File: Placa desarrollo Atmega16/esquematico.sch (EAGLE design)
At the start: 34 parts, among them IC1 MEGA16-P, IC2 7805DT, IC3 7805DT, Q1 16MHz

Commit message: PCB sin rutear
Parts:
- removed C13: 100nF, rcl:C-EUC1206
- removed C14: 10uF, rcl:CPOL-EUE2,5-6E
- removed Q1: 16MHz, crystal:CRYSTALHC33U-V
- added JP2: (no value), jumper:JP1E
- added Q2: 16MHz, crystal:CRYSTALHC49S
- added X1: PN61729-S, con-berg:PN61729-S
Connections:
- removed net N$4: R5.2
- removed net N$7: C13.1, C14.+, IC2.VI
- new net PA6: IC1.(ADC6)PA6, SV2.14
- net AREF: now also SV2.12
- net GND: now also SV2.11, X1.4, X1.S1, X1.S2; no longer C13.2, C14.-
- net N$5: now also IC2.VI, JP2.2; no longer C10.+, C9.1
- net PA0: now also SV2.20
- net PA1: now also SV2.19
- net PA2: now also SV2.18
- net PA3: now also SV2.17
- net PA4: now also SV2.16
- net PA5: now also SV2.15
- net PA7: now also SV2.13; no longer IC1.(ADC6)PA6
- net PC0: now also SV2.2
- net PC1: now also SV2.3
- net PC2: now also SV2.4
- net PC3: now also SV2.5
- net PC4: now also SV2.6
- net PC5: now also SV2.7
- net PC6: now also SV2.8
- net PC7: now also SV2.9
- net PD7: now also SV2.1
- net VCC_5V: now also C10.+, C9.1, R5.2, SV2.10, X1.1
- net VIN: now also JP2.1
- net XTAL1: now also Q2.1; no longer Q1.2
- net XTAL2: now also Q2.2; no longer Q1.1
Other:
- moved on the sheet: R5

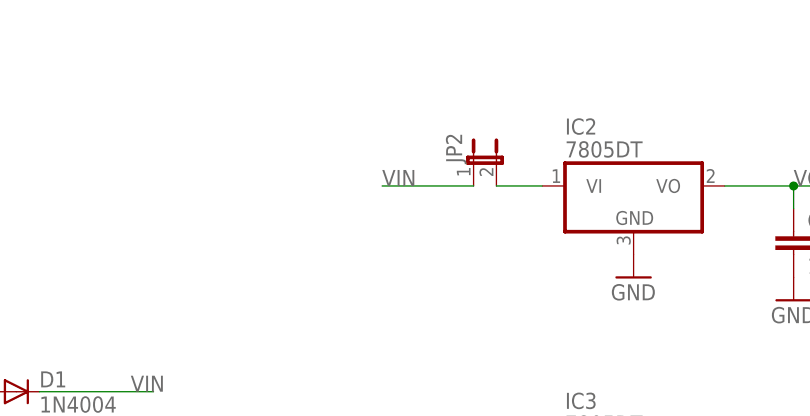
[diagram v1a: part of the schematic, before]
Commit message: Modifique el jumper del lm7833
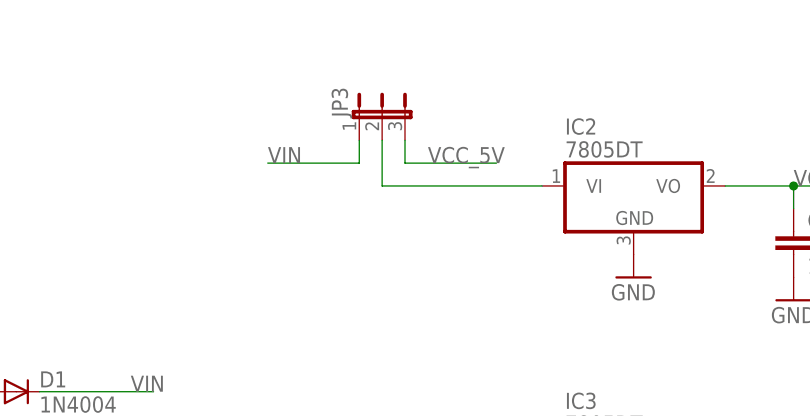
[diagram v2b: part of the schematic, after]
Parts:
- removed JP2: (no value), jumper:JP1E
- added JP3: (no value), jumper:JP2E
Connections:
- net N$5: now also JP3.2; no longer JP2.2
- net VCC_5V: now also JP3.3
- net VIN: now also JP3.1; no longer JP2.1
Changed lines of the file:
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@@
 <part name="GND22" library="supply1" deviceset="GND" device=""/>
 <part name="Q2" library="crystal" deviceset="CRYSTAL" device="HC49S" value="16MHz"/>
-<part name="JP2" library="jumper" deviceset="JP1E" device=""/>
+<part name="JP3" library="jumper" deviceset="JP2E" device=""/>
 </parts>
 <sheets>
@@
 <instance part="GND22" gate="1" x="-48.26" y="149.86"/>
 <instance part="Q2" gate="G$1" x="-38.1" y="58.42"/>
-<instance part="JP2" gate="A" x="15.24" y="147.32"/>
+<instance part="JP3" gate="1" x="5.08" y="152.4"/>
 </instances>
 <busses>
@@
 <label x="-25.4" y="27.94" size="1.778" layer="95"/>
 </segment>
+<segment>
+<pinref part="JP3" gate="1" pin="3"/>
+<wire x1="7.62" y1="149.86" x2="7.62" y2="147.32" width="0.1524" layer="91"/>
+<wire x1="7.62" y1="147.32" x2="17.78" y2="147.32" width="0.1524" layer="91"/>
+<label x="10.16" y="147.32" size="1.778" layer="95"/>
+</segment>
 </net>
 <net name="MOSI" class="0">
@@
 </segment>
 <segment>
-<pinref part="JP2" gate="A" pin="1"/>
-<wire x1="15.24" y1="144.78" x2="5.08" y2="144.78" width="0.1524" layer="91"/>
-<label x="5.08" y="144.78" size="1.778" layer="95"/>
+<wire x1="2.54" y1="147.32" x2="-7.62" y2="147.32" width="0.1524" layer="91"/>
+<label x="-7.62" y="147.32" size="1.778" layer="95"/>
+<pinref part="JP3" gate="1" pin="1"/>
+<wire x1="2.54" y1="149.86" x2="2.54" y2="147.32" width="0.1524" layer="91"/>
 </segment>
 </net>
@@
 <net name="N$5" class="0">
 <segment>
-<pinref part="JP2" gate="A" pin="2"/>
 <pinref part="IC2" gate="A1" pin="VI"/>
-<wire x1="17.78" y1="144.78" x2="22.86" y2="144.78" width="0.1524" layer="91"/>
-</segment>
-</net>
+<pinref part="JP3" gate="1" pin="2"/>
+<wire x1="5.08" y1="149.86" x2="5.08" y2="144.78" width="0.1524" layer="91"/>
+<wire x1="5.08" y1="144.78" x2="22.86" y2="144.78" width="0.1524" layer="91"/>
+</segment>
+</net>

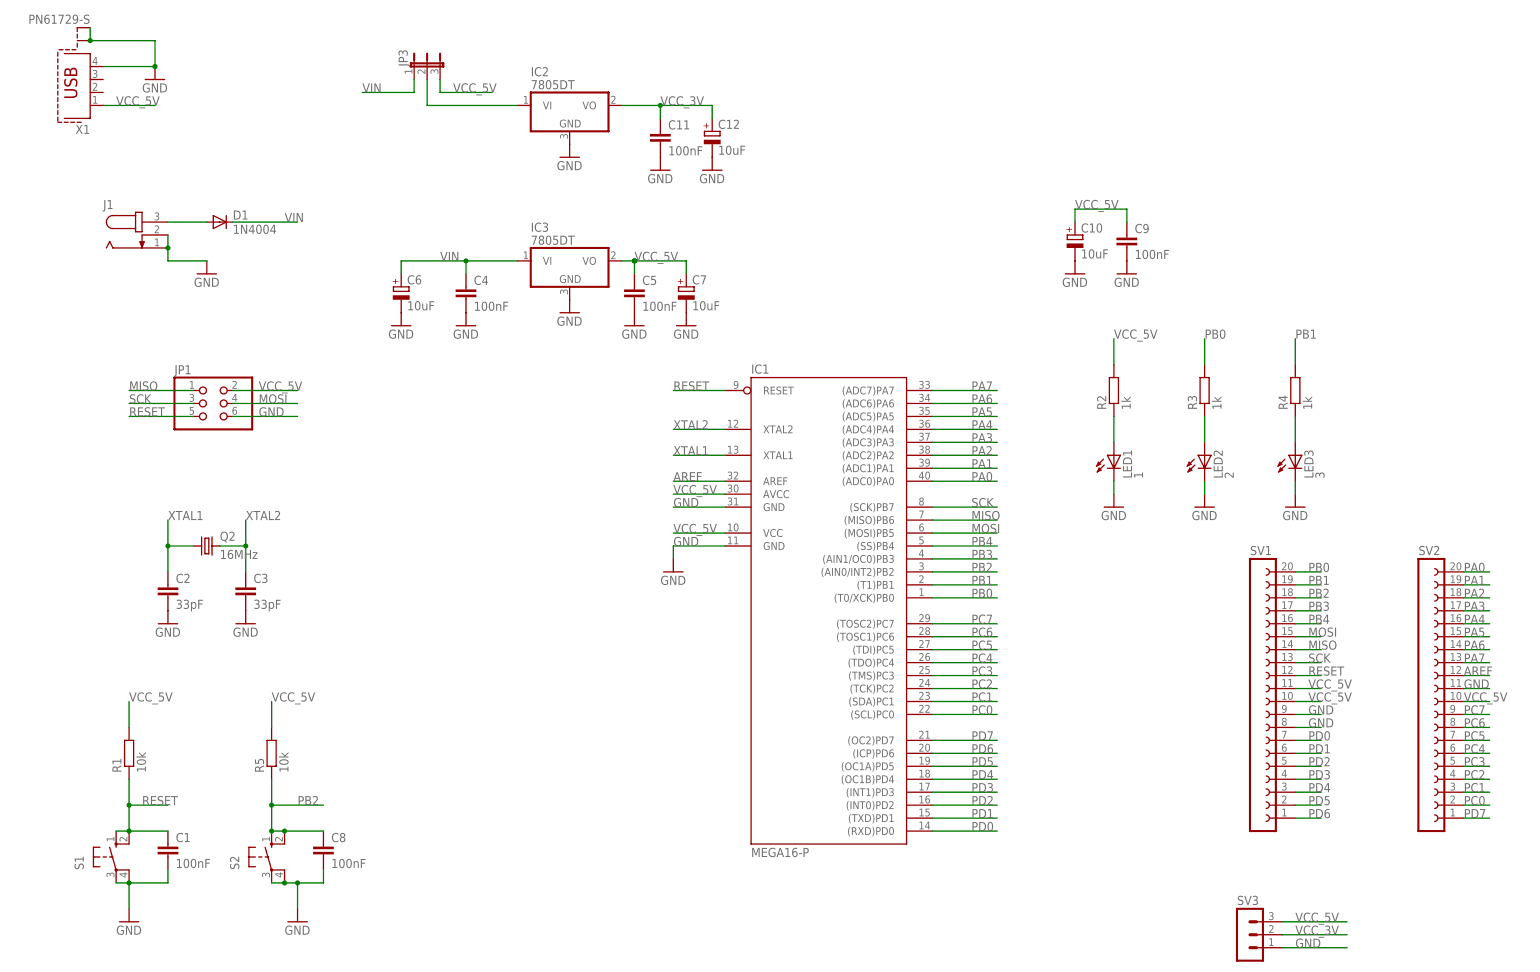
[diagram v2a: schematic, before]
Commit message: Modifique el ancho de las pistas. Hay algunos problemas con la interconexion de masas
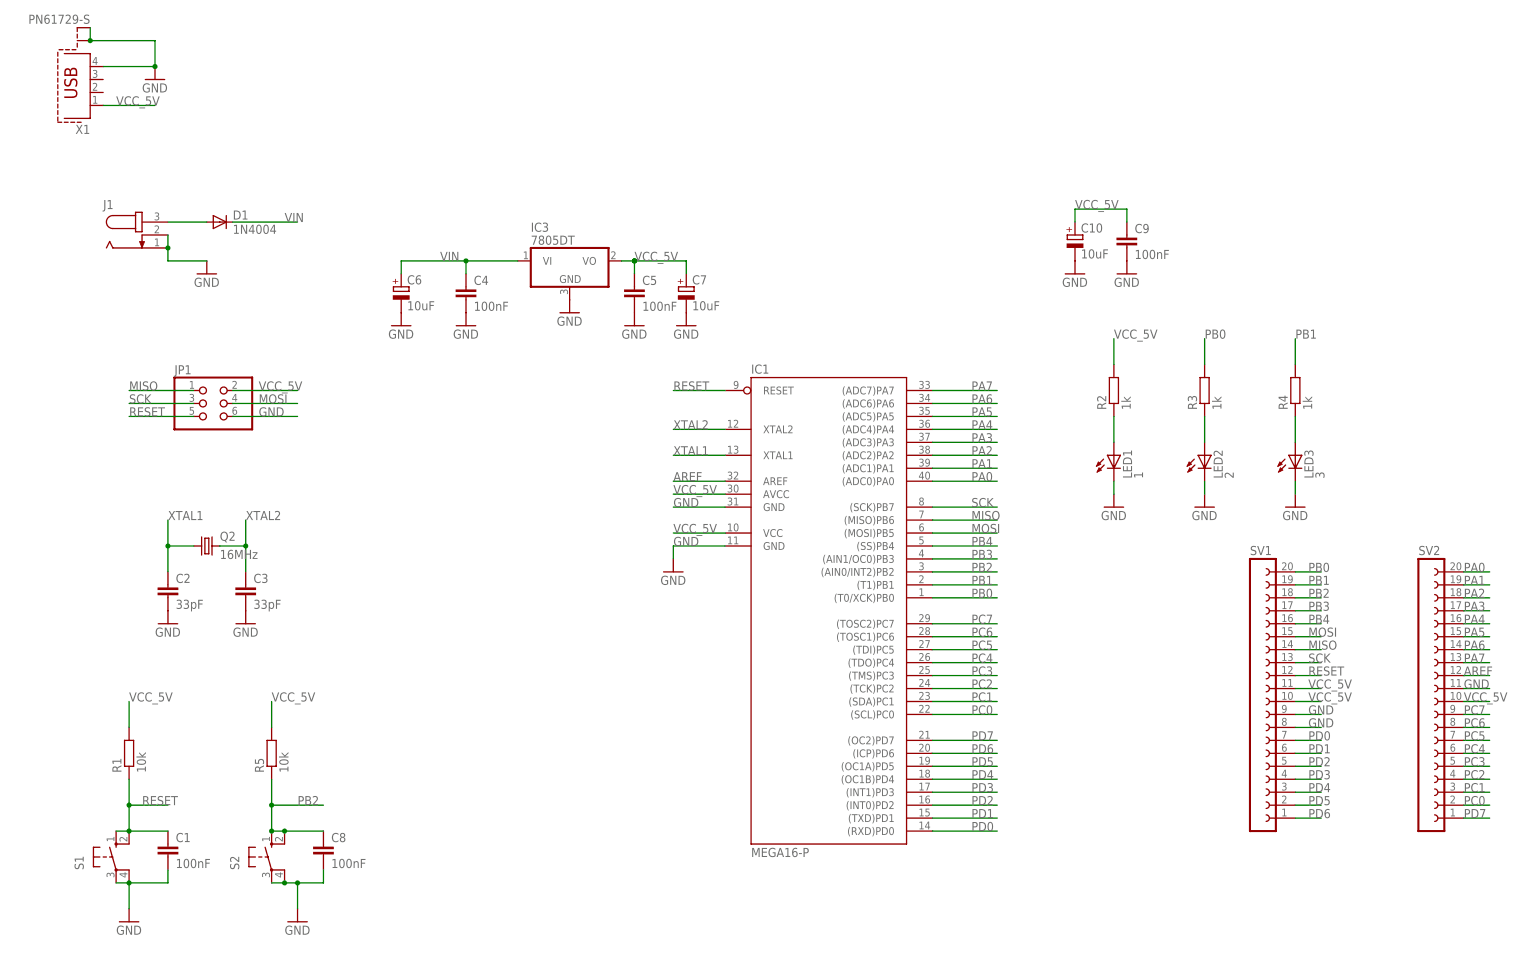
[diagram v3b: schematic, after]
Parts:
- removed C11: 100nF, rcl:C-EUC1206
- removed C12: 10uF, rcl:CPOL-EUE2,5-6E
- removed IC2: 7805DT, linear:7805DT
- removed JP3: (no value), jumper:JP2E
- removed SV3: (no value), con-lstb:MA03-1
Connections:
- removed net N$5: IC2.VI, JP3.2
- removed net VCC_3V: C11.1, C12.+, IC2.VO, SV3.2
- net GND: no longer C11.2, C12.-, IC2.GND, SV3.1
- net VCC_5V: no longer JP3.3, SV3.3
- net VIN: no longer JP3.1
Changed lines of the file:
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@@
 <part name="D1" library="diode" deviceset="1N4004" device=""/>
 <part name="IC3" library="linear" deviceset="78*" device="DT" technology="05"/>
-<part name="IC2" library="linear" deviceset="78*" device="DT" technology="05"/>
-<part name="GND17" library="supply1" deviceset="GND" device=""/>
-<part name="C11" library="rcl" deviceset="C-EU" device="C1206" value="100nF"/>
-<part name="C12" library="rcl" deviceset="CPOL-EU" device="E2,5-6E" value="10uF"/>
-<part name="GND20" library="supply1" deviceset="GND" device=""/>
-<part name="GND21" library="supply1" deviceset="GND" device=""/>
-<part name="SV3" library="con-lstb" deviceset="MA03-1" device=""/>
 <part name="X1" library="con-berg" deviceset="PN61729-S" device=""/>
 <part name="GND22" library="supply1" deviceset="GND" device=""/>
 <part name="Q2" library="crystal" deviceset="CRYSTAL" device="HC49S" value="16MHz"/>
-<part name="JP3" library="jumper" deviceset="JP2E" device=""/>
 </parts>
 <sheets>
@@
 <instance part="D1" gate="1" x="-35.56" y="121.92"/>
 <instance part="IC3" gate="A1" x="33.02" y="114.3"/>
-<instance part="IC2" gate="A1" x="33.02" y="144.78"/>
-<instance part="GND17" gate="1" x="33.02" y="134.62"/>
-<instance part="C11" gate="G$1" x="50.8" y="139.7"/>
-<instance part="C12" gate="G$1" x="60.96" y="139.7"/>
-<instance part="GND20" gate="1" x="50.8" y="132.08"/>
-<instance part="GND21" gate="1" x="60.96" y="132.08"/>
-<instance part="SV3" gate="G$1" x="165.1" y="-17.78"/>
 <instance part="X1" gate="G$1" x="-60.96" y="149.86" rot="R180"/>
 <instance part="GND22" gate="1" x="-48.26" y="149.86"/>
 <instance part="Q2" gate="G$1" x="-38.1" y="58.42"/>
-<instance part="JP3" gate="1" x="5.08" y="152.4"/>
 </instances>
 <busses>
@@
 </segment>
 <segment>
-<pinref part="SV3" gate="G$1" pin="3"/>
-<wire x1="172.72" y1="-15.24" x2="185.42" y2="-15.24" width="0.1524" layer="91"/>
-<label x="175.26" y="-15.24" size="1.778" layer="95"/>
-</segment>
-<segment>
 <pinref part="SV2" gate="G$1" pin="10"/>
 <wire x1="208.28" y1="27.94" x2="213.36" y2="27.94" width="0.1524" layer="91"/>
@@
 <wire x1="-25.4" y1="22.86" x2="-25.4" y2="27.94" width="0.1524" layer="91"/>
 <label x="-25.4" y="27.94" size="1.778" layer="95"/>
-</segment>
-<segment>
-<pinref part="JP3" gate="1" pin="3"/>
-<wire x1="7.62" y1="149.86" x2="7.62" y2="147.32" width="0.1524" layer="91"/>
-<wire x1="7.62" y1="147.32" x2="17.78" y2="147.32" width="0.1524" layer="91"/>
-<label x="10.16" y="147.32" size="1.778" layer="95"/>
 </segment>
 </net>
@@
 </segment>
 <segment>
-<pinref part="IC2" gate="A1" pin="GND"/>
-<pinref part="GND17" gate="1" pin="GND"/>
-</segment>
-<segment>
-<pinref part="C11" gate="G$1" pin="2"/>
-<pinref part="GND20" gate="1" pin="GND"/>
-</segment>
-<segment>
-<pinref part="C12" gate="G$1" pin="-"/>
-<pinref part="GND21" gate="1" pin="GND"/>
-</segment>
-<segment>
-<pinref part="SV3" gate="G$1" pin="1"/>
-<wire x1="172.72" y1="-20.32" x2="185.42" y2="-20.32" width="0.1524" layer="91"/>
-<label x="175.26" y="-20.32" size="1.778" layer="95"/>
-</segment>
-<segment>
 <pinref part="X1" gate="G$1" pin="4"/>
 <wire x1="-58.42" y1="152.4" x2="-48.26" y2="152.4" width="0.1524" layer="91"/>
@@
 <wire x1="-33.02" y1="121.92" x2="-20.32" y2="121.92" width="0.1524" layer="91"/>
 <label x="-22.86" y="121.92" size="1.778" layer="95"/>
-</segment>
-<segment>
-<wire x1="2.54" y1="147.32" x2="-7.62" y2="147.32" width="0.1524" layer="91"/>
-<label x="-7.62" y="147.32" size="1.778" layer="95"/>
-<pinref part="JP3" gate="1" pin="1"/>
-<wire x1="2.54" y1="149.86" x2="2.54" y2="147.32" width="0.1524" layer="91"/>
 </segment>
 </net>
@@
 </segment>
 </net>
-<net name="VCC_3V" class="0">
-<segment>
-<pinref part="IC2" gate="A1" pin="VO"/>
-<wire x1="43.18" y1="144.78" x2="50.8" y2="144.78" width="0.1524" layer="91"/>
-<pinref part="C12" gate="G$1" pin="+"/>
-<wire x1="50.8" y1="144.78" x2="60.96" y2="144.78" width="0.1524" layer="91"/>
-<wire x1="60.96" y1="144.78" x2="60.96" y2="142.24" width="0.1524" layer="91"/>
-<pinref part="C11" gate="G$1" pin="1"/>
-<wire x1="50.8" y1="142.24" x2="50.8" y2="144.78" width="0.1524" layer="91"/>
-<junction x="50.8" y="144.78"/>
-<label x="50.8" y="144.78" size="1.778" layer="95"/>
-</segment>
-<segment>
-<pinref part="SV3" gate="G$1" pin="2"/>
-<wire x1="172.72" y1="-17.78" x2="185.42" y2="-17.78" width="0.1524" layer="91"/>
-<label x="175.26" y="-17.78" size="1.778" layer="95"/>
-</segment>
-</net>
 <net name="PA6" class="0">
 <segment>
@@
 </segment>
 </net>
-<net name="N$5" class="0">
-<segment>
-<pinref part="IC2" gate="A1" pin="VI"/>
-<pinref part="JP3" gate="1" pin="2"/>
-<wire x1="5.08" y1="149.86" x2="5.08" y2="144.78" width="0.1524" layer="91"/>
-<wire x1="5.08" y1="144.78" x2="22.86" y2="144.78" width="0.1524" layer="91"/>
-</segment>
-</net>

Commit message: Supuestamente corregi el tema de las masas
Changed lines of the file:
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@@
 <junction x="45.72" y="114.3"/>
 <wire x1="45.72" y1="114.3" x2="55.88" y2="114.3" width="0.1524" layer="91"/>
-<label x="132.08" y="124.46" size="1.778" layer="95"/>
 <pinref part="IC3" gate="A1" pin="VO"/>
 </segment>
@@
 <pinref part="C9" gate="G$1" pin="1"/>
 <wire x1="142.24" y1="124.46" x2="142.24" y2="121.92" width="0.1524" layer="91"/>
+<label x="132.08" y="121.92" size="1.778" layer="95"/>
+<label x="142.24" y="121.92" size="1.778" layer="95"/>
 </segment>
 <segment>
